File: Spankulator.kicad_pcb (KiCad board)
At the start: 4 copper layers, 50.5 x 110 mm, 97 parts, among them J1 3.5mm Jack, J2 2X8 Header, J3 3.5mm Jack, J4 3.5mm Jack, J5 3.5mm Jack, J6 3.5mm Jack, J7 Expansion Header, J8 FRAM Header, J9 Display Header, Q1 ZVN4206A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

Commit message: v2.2.3
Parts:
- added Q6: TN2106, digikey-footprints:TO-92-3_Formed_Leads, F.Cu at (113.0, 142.1)
- added R21: 10K, Resistor_THT:R_Axial_DIN0207_L6.3mm_D2.5mm_P10.16mm_Horizontal, F.Cu at (113.0, 134.0)
- Q1: value ZVN4206A -> TN2106
- Q2, Q3, Q4, Q5: footprint Package_TO_SOT_THT:TO-92_Inline -> Package_TO_SOT_THT:TO-92_HandSolder
- RV1: value 10K -> 1K
- moved D15 15.4 mm to (58.0, 132.8), turned to 270 degrees
- moved RV1 10.5 mm to (71.1, 144.0), turned to 90 degrees
- moved D3 2.54 mm to (106.2, 48.0), turned to 0 degrees
- moved D4 2.54 mm to (106.2, 78.0), turned to 0 degrees
- moved C13 2.47 mm to (76.6, 132.8)
- moved C3 2.25 mm to (64.0, 51.2)
- moved Q2 0.25 mm to (86.3, 65.5)
- moved Q5 0.20 mm to (86.3, 54.4)
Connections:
- D3 pad 1: GND -> Net-(D3-Pad1)
- D3 pad 2: Net-(D3-Pad2) -> +3V3
- D4 pad 1: GND -> Net-(D4-Pad1)
- D4 pad 2: Net-(D4-Pad2) -> +3V3
- J7 pad 1: Net-(A1-Pad16) -> Net-(J7-Pad1)
- R2 pad 2: Net-(D3-Pad2) -> Net-(D3-Pad1)
- R3 pad 2: Net-(D4-Pad2) -> Net-(D4-Pad1)
- U2 pad 5: +5V -> Net-(Q6-Pad3)
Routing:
- net Net-(A1-Pad16): track 92.9 -> 38.5 mm
- net Net-(D3-Pad2): track 45.4 -> 0.00 mm, vias 2 -> 0
- net Net-(D3-Pad1): track 0.00 -> 45.4 mm, vias 0 -> 2
- net Net-(D4-Pad2): track 44.3 -> 0.00 mm, vias 1 -> 0
- net Net-(D4-Pad1): track 0.00 -> 44.3 mm, vias 0 -> 1
- net Net-(Q6-Pad3): track 0.00 -> 20.2 mm
- net Net-(A1-Pad21): track 80.0 -> 99.6 mm, vias 5 -> 6
- net Net-(A1-Pad20): track 69.5 -> 83.4 mm, vias 1 -> 2
- net +3V3: track 79.7 -> 92.4 mm, vias 10 -> 11
- net /Down: track 103.5 -> 95.5 mm
- net +5V: track 242.3 -> 239.6 mm, vias 7 -> 6
- net /Up: track 116.4 -> 114.1 mm
- net Net-(Q4-Pad2): track 3.39 -> 4.66 mm
- net Net-(Q3-Pad2): track 5.00 -> 6.27 mm
- net Net-(Q2-Pad2): track 9.11 -> 7.84 mm
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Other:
- board size 50.5 x 110 mm -> 60.4 x 110 mm
- board text added: "v2.2"
- board text removed: "v2.1"

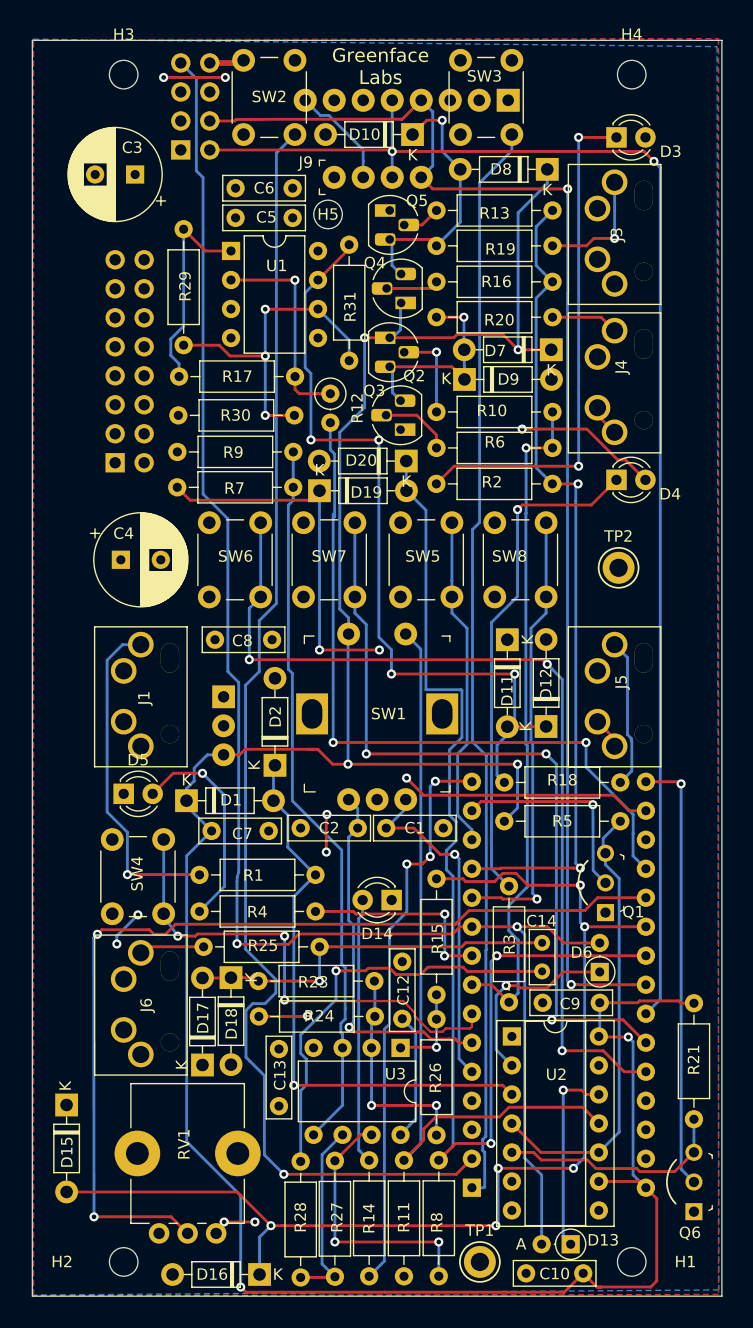
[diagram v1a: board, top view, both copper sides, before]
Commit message: This version adds separate control of external trigger enable. Now uses full-width main board.
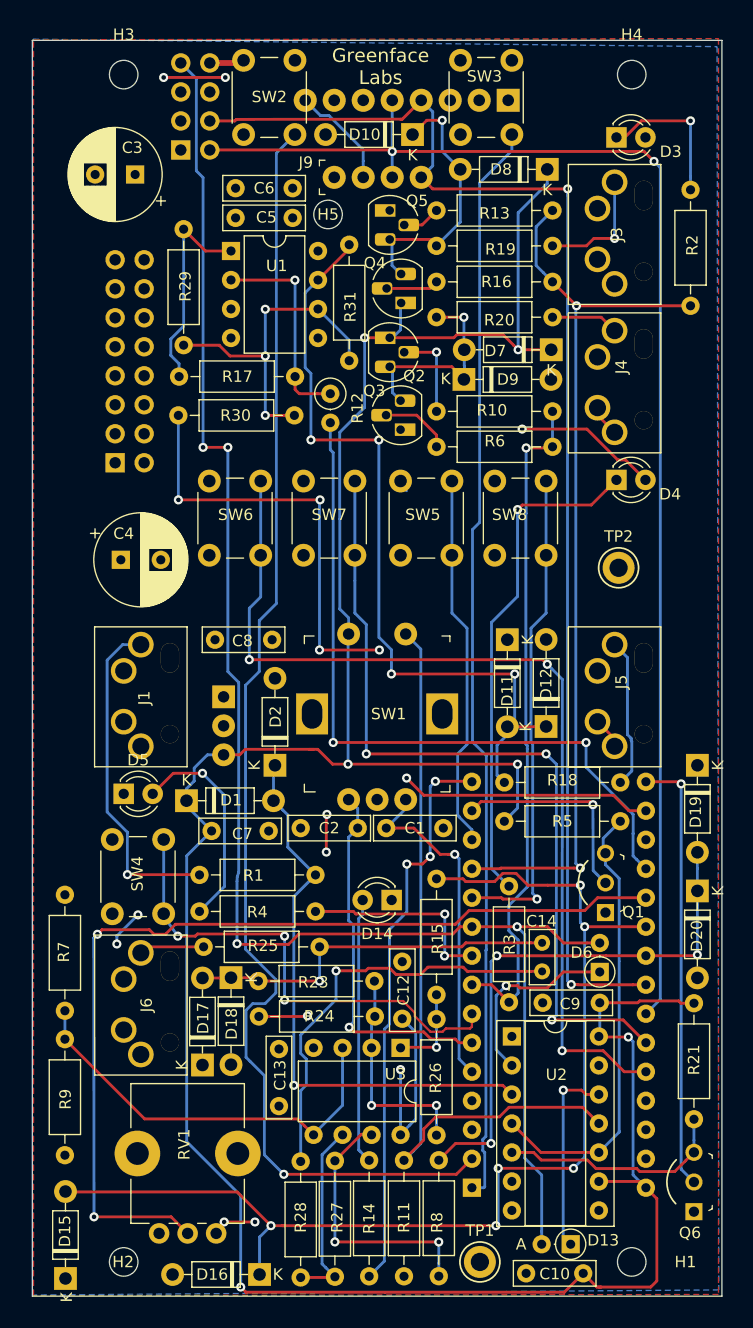
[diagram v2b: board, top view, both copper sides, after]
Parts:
- moved R9 62.4 mm to (57.9, 137.2), turned to 90 degrees
- moved R7 50.0 mm to (57.9, 124.5), turned to 90 degrees
- moved D20 45.5 mm to (113.2, 114.0), turned to 270 degrees
- moved D19 40.9 mm to (113.2, 103.0), turned to 270 degrees
- moved R2 19.7 mm to (112.7, 62.8), turned to 90 degrees
- moved D15 15.2 mm to (57.9, 147.9), turned to 90 degrees
- moved SW5 3.65 mm to (87.2, 84.6)
- moved SW6 3.65 mm to (70.5, 84.6)
- moved SW7 3.65 mm to (78.8, 84.6)
- moved SW8 3.65 mm to (95.5, 84.6)
- moved R6 0.10 mm to (90.4, 75.1)
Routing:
- net Net-(A1-Pad22): track 101.8 -> 48.4 mm, vias 2 -> 3
- net Net-(D3-Pad1): track 45.4 -> 13.4 mm, vias 2 -> 1
- net 1.65V: track 63.3 -> 36.4 mm
- net Net-(A1-Pad12): track 72.1 -> 79.4 mm
- net +3V3: track 92.4 -> 98.1 mm, vias 11 -> 13
- net +12V: track 14.5 -> 20.2 mm, vias 2 -> 3
- net /Param+: track 39.5 -> 44.3 mm
- net /Param-: track 29.2 -> 32.8 mm
- net /Right: track 81.2 -> 84.8 mm
- net /Left: track 69.3 -> 73.0 mm
- net /Trigger: track 141.0 -> 142.3 mm, vias 2 -> 4

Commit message: Ver 2.3
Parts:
- added H6: MountingHole, sputterizer:MountingHole_2.5mm-No-Margin, F.Cu at (73.5, 76.0)
- added H7: MountingHole, sputterizer:MountingHole_2.5mm-No-Margin, F.Cu at (96.8, 76.0)
- D13, D6: footprint Diode_THT:D_DO-35_SOD27_P2.54mm_Vertical_AnodeUp -> Diode_THT:D_DO-35_SOD27_P7.62mm_Horizontal
- R12: footprint Resistor_THT:R_Axial_DIN0207_L6.3mm_D2.5mm_P2.54mm_Vertical -> Resistor_THT:R_Axial_DIN0207_L6.3mm_D2.5mm_P10.16mm_Horizontal
- moved R6 23.3 mm to (112.7, 82.1), turned to 90 degrees
- moved D6 22.9 mm to (113.1, 99.8)
- moved TP1 18.4 mm to (112.6, 146.6)
- moved R12 17.8 mm to (66.5, 60.2)
- moved R17 13.5 mm to (69.6, 55.6), turned to 270 degrees
- moved R29 11.7 mm to (79.7, 68.8), turned to 180 degrees
- moved J2 4.14 mm to (58.1, 76.1)
- moved R30 1.84 mm to (79.7, 71.8)
- moved SW5 1.00 mm to (87.2, 85.6)
- moved SW6 1.00 mm to (70.5, 85.6)
- moved SW7 1.00 mm to (78.8, 85.6)
- moved SW8 1.00 mm to (95.5, 85.6)
- moved D13 0.65 mm to (101.5, 145.0)
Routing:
- net /Trigger: track 142.3 -> 189.6 mm, vias 4 -> 6
- net Net-(D6-Pad1): track 16.8 -> 45.6 mm, vias 1 -> 2
- net +3V3: track 98.1 -> 69.7 mm, vias 13 -> 8
- net Net-(Q3-Pad2): track 6.27 -> 34.4 mm, vias 0 -> 1
- net Net-(R29-Pad1): track 29.7 -> 12.3 mm, vias 3 -> 0
- net Net-(A1-Pad19): track 64.2 -> 81.5 mm, vias 2 -> 3
- net Net-(A1-Pad8): track 59.3 -> 71.5 mm, vias 1 -> 0
- net +5V: track 239.6 -> 232.3 mm
- net Net-(R12-Pad1): track 18.4 -> 12.4 mm, vias 1 -> 0
- net /Param+: track 44.3 -> 43.1 mm
- net Net-(D11-Pad2): track 70.1 -> 70.8 mm
- net Net-(D4-Pad1): track 44.3 -> 45.0 mm
- net Net-(R17-Pad1): track 18.6 -> 18.1 mm
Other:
- board text added: "v2.3"
- board text removed: "v2.2"

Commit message: ver 3.0
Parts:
- removed D10, D17, D18, D2, D9: SB120, sputterizer:D_DO-41_SOD27_P7.62mm_Horizontal
- removed Q2, Q4: 2N3906, Package_TO_SOT_THT:TO-92_HandSolder
- removed R13: 100K, Resistor_THT:R_Axial_DIN0207_L6.3mm_D2.5mm_P10.16mm_Horizontal
- removed R25: 470, Resistor_THT:R_Axial_DIN0207_L6.3mm_D2.5mm_P10.16mm_Horizontal
- added C11: 2.2uF, Capacitor_THT:C_Rect_L7.0mm_W2.0mm_P5.00mm, F.Cu at (56.9, 109.6)
- added C15: 2.2uF, Capacitor_THT:C_Rect_L7.0mm_W2.0mm_P5.00mm, F.Cu at (57.3, 101.5)
- added C16: 270p, Capacitor_THT:C_Rect_L4.0mm_W2.5mm_P2.50mm, F.Cu at (65.5, 78.6)
- added C17: 100nF, Capacitor_THT:C_Rect_L7.0mm_W2.0mm_P5.00mm, F.Cu at (57.5, 78.4)
- added U5: LP2950-3.3_TO92, Package_TO_SOT_THT:TO-92_Inline, F.Cu at (58.4, 106.8)
- added U6: MAX7480, Package_DIP:DIP-8_W7.62mm_Socket_LongPads, F.Cu at (57.5, 81.5)
- A1: value Arduino_Nano_33IoT -> Nano_33IoT
- D1, D15, D16, D19, D20: value SB120 -> BAT46; footprint sputterizer:D_DO-41_SOD27_P7.62mm_Horizontal -> Diode_THT:D_DO-35_SOD27_P7.62mm_Horizontal
- J2: value 2X8 Header -> 2x5 Header; footprint Connector_PinHeader_2.54mm:PinHeader_2x08_P2.54mm_Vertical -> Connector_PinHeader_2.54mm:PinHeader_2x05_P2.54mm_Vertical
- Q3, Q5: value 2N3904 -> TN2106; footprint Package_TO_SOT_THT:TO-92_HandSolder -> digikey-footprints:TO-92-3_Formed_Leads
- R10, R16: value 47K -> 470
- R12, R26, R27: value 100K -> 100K .1%
- R29, R31: value 200K -> 100K .1%
- R30: value 133K -> 100K .1%
- R6: value 100K -> 10K
- R7, R9: value 470 -> 510 .1%
- SW2, SW3, SW4, SW5, SW6, SW7, SW8: value ~ -> Push Button
- TP2: moved to B.Cu
- moved R8 60.0 mm to (80.2, 88.7), turned to 180 degrees
- moved J8 55.8 mm to (113.5, 98.0), turned to 90 degrees
- moved D1 44.8 mm to (113.2, 104.0), turned to 270 degrees
- moved TP2 41.0 mm to (101.6, 44.9)
- moved D20 38.1 mm to (76.0, 106.0), turned to 180 degrees
- moved D19 38.0 mm to (75.9, 96.0)
- moved H5 35.6 mm to (103.5, 82.2), turned to 270 degrees
- moved C14 28.4 mm to (72.2, 126.0)
- moved C4 26.9 mm to (58.0, 58.5)
- moved D6 21.7 mm to (113.2, 121.5)
- moved R6 19.0 mm to (94.9, 88.8), turned to 0 degrees
- moved R10 15.2 mm to (100.6, 60.7), turned to 180 degrees
- moved R31 11.3 mm to (82.8, 68.7), turned to 90 degrees
- moved R7 11.0 mm to (57.0, 135.5)
- moved R9 10.9 mm to (57.0, 148.0)
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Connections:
- A1 pad 18: Net-(A1-Pad18) -> 3.3VRef
- A1 pad 21: Net-(A1-Pad21) -> SigIn
- A1 pad 3: Net-(A1-Pad3) -> Reset
- D1 pad 1: +5V -> +3V3
- D1 pad 2: Net-(D1-Pad2) -> Net-(A1-Pad22)
- D15 pad 2: Net-(A1-Pad21) -> SigIn
- D16 pad 1: Net-(A1-Pad21) -> SigIn
- D19 pad 1: +3V3 -> +5V
- D19 pad 2: Net-(A1-Pad22) -> Net-(D19-Pad2)
- D20 pad 1: Net-(A1-Pad22) -> Net-(D19-Pad2)
- D8 pad 2: Net-(D10-Pad1) -> Net-(D8-Pad2)
- J6 pad 2: Net-(J6-Pad2) -> Net-(C14-Pad1)
- J7 pad 1: Net-(J7-Pad1) -> Reset
- J7 pad 3: +3V3 -> SigIn
- Q3 pad 2: Net-(Q3-Pad2) -> Net-(A1-Pad8)
- Q5 pad 2: Net-(Q5-Pad2) -> Net-(A1-Pad12)
- Q5 pad 3: Net-(D10-Pad1) -> Net-(D8-Pad2)
- R1 pad 1: Net-(D1-Pad2) -> Net-(R1-Pad1)
- R10 pad 1: Net-(Q2-Pad2) -> +5V
- R10 pad 2: Net-(A1-Pad8) -> Net-(D7-Pad2)
- R15 pad 2: Net-(A1-Pad21) -> SigIn
- R16 pad 1: Net-(Q4-Pad2) -> +5V
- R16 pad 2: Net-(A1-Pad12) -> Net-(D8-Pad2)
- R17 pad 1: Net-(R17-Pad1) -> Net-(D11-Pad2)
- R19 pad 1: Net-(D10-Pad1) -> Net-(D8-Pad2)
- R24 pad 2: +3V3 -> 3.3VRef
- R29 pad 2: Net-(R17-Pad1) -> 1.65V
- R30 pad 1: Net-(R29-Pad1) -> Net-(R12-Pad1)
- R30 pad 2: +3V3 -> Net-(R30-Pad2)
- R31 pad 1: Net-(D11-Pad2) -> Net-(R30-Pad2)
- R6 pad 1: Net-(Q3-Pad2) -> Net-(R6-Pad1)
- R6 pad 2: Net-(A1-Pad8) -> Net-(A1-Pad22)
- R7 pad 2: +3V3 -> 3.3VRef
- R8 pad 2: Net-(A1-Pad22) -> Net-(D19-Pad2)
- RV1 pad 1: +3V3 -> 3.3VRef
- U1 pad 1: Net-(R17-Pad1) -> Net-(D11-Pad2)
- U1 pad 7: Net-(D11-Pad2) -> Net-(R30-Pad2)
- U2 pad 3: Net-(D1-Pad2) -> Net-(R1-Pad1)
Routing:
- net SigIn: track 0.00 -> 170.0 mm, vias 0 -> 7
- net Reset: track 0.00 -> 109.7 mm, vias 0 -> 2
- net 3.3VRef: track 0.00 -> 103.5 mm, vias 0 -> 1
- net Net-(A1-Pad21): track 99.6 -> 0.00 mm, vias 6 -> 0
- net 1.65V: track 36.4 -> 122.9 mm, vias 0 -> 3
- net +3V3: track 69.7 -> 13.7 mm, vias 8 -> 5
- net Net-(D1-Pad2): track 49.8 -> 0.00 mm, vias 1 -> 0
- net Net-(R1-Pad1): track 0.00 -> 38.6 mm, vias 0 -> 1
- net Net-(D19-Pad2): track 0.00 -> 38.0 mm, vias 0 -> 1
- net Net-(Q3-Pad2): track 34.4 -> 0.00 mm, vias 1 -> 0
- net Net-(R27-Pad2): track 23.5 -> 55.8 mm, vias 2 -> 0
- net Net-(R6-Pad1): track 0.00 -> 30.4 mm
- net /Trigger: track 189.6 -> 165.5 mm
- net Net-(D10-Pad1): track 23.1 -> 0.00 mm, vias 1 -> 0
- net Net-(C14-Pad2): track 37.2 -> 14.4 mm
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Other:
- board text added: "v3.0"
- board text removed: "Pin 1 -12V"
- board text removed: "v2.3"

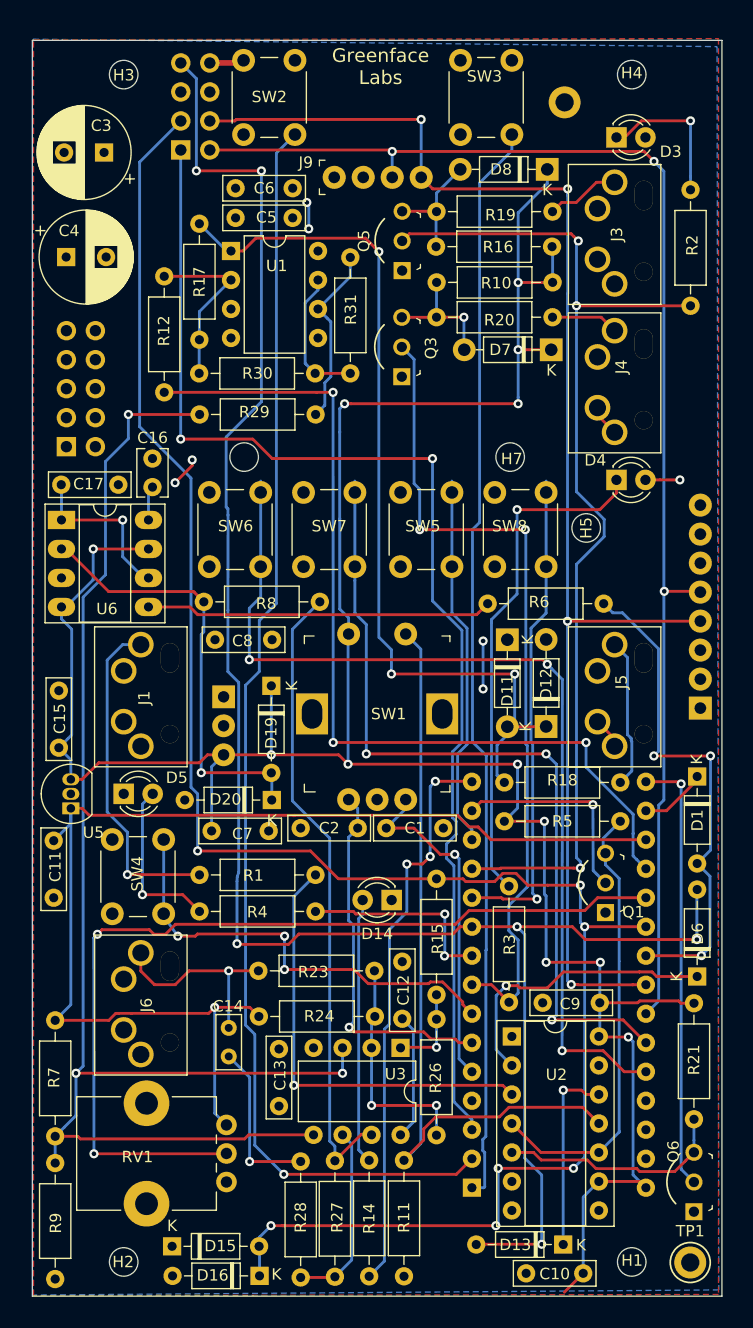
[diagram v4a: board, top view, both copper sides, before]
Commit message: Version 3.1
Adds adjustment pots.
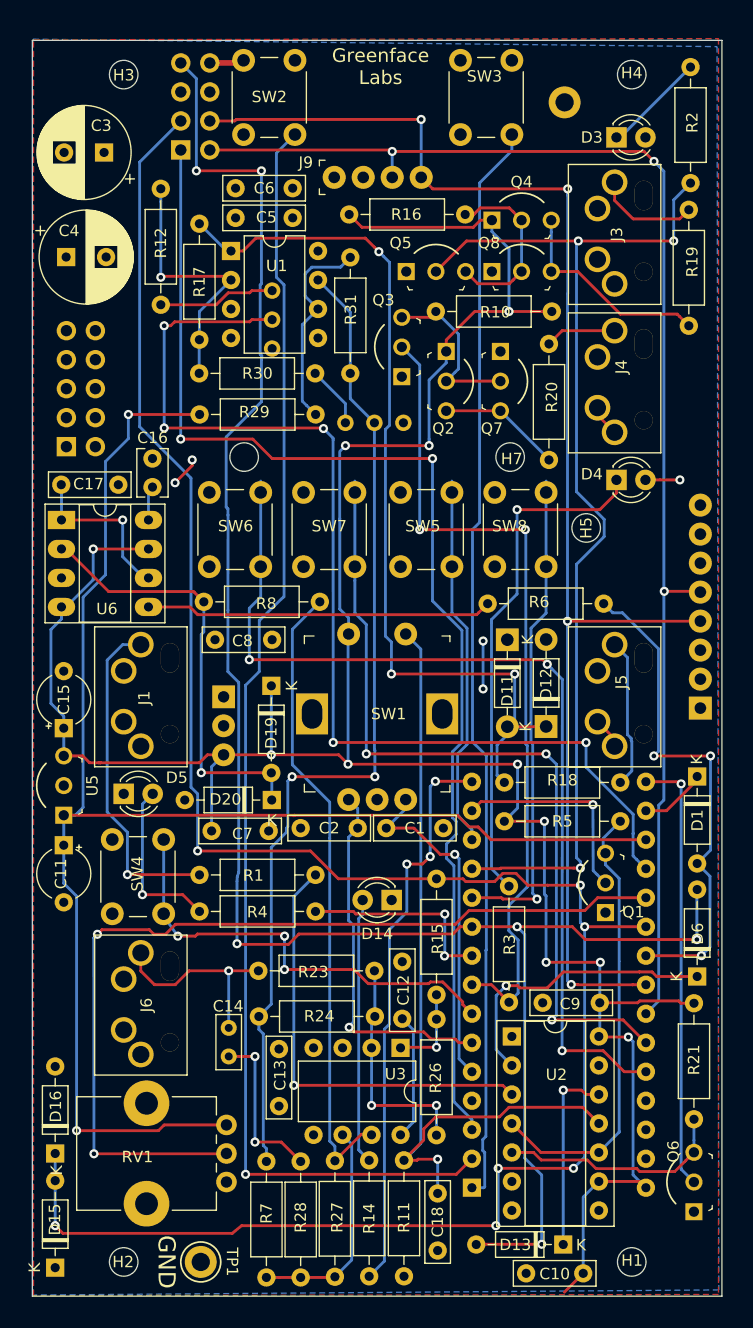
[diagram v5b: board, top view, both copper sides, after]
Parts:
- removed D7, D8: SB120, sputterizer:D_DO-41_SOD27_P7.62mm_Horizontal
- removed R9: 510 .1%, Resistor_THT:R_Axial_DIN0207_L6.3mm_D2.5mm_P10.16mm_Horizontal
- added C18: 10nF, Capacitor_THT:C_Rect_L7.0mm_W2.0mm_P5.00mm, F.Cu at (90.5, 140.5)
- added Q2: VP2106, digikey-footprints:TO-92-3_Formed_Leads, F.Cu at (91.2, 66.8)
- added Q4: VP2106, digikey-footprints:TO-92-3_Formed_Leads, F.Cu at (95.2, 55.2)
- added Q7: TN2106, digikey-footprints:TO-92-3_Formed_Leads, F.Cu at (96.0, 66.8)
- added Q8: TN2106, digikey-footprints:TO-92-3_Formed_Leads, F.Cu at (95.2, 59.8)
- added RV2: 10K, Potentiometer_THT:Potentiometer_Bourns_3266Y_Vertical, B.Cu at (76.0, 66.5)
- added RV3: 10K, Potentiometer_THT:Potentiometer_Bourns_3266Y_Vertical, B.Cu at (87.5, 73.0)
- C11, C15: footprint Capacitor_THT:C_Rect_L7.0mm_W2.0mm_P5.00mm -> sputterizer:CP_Radial_Tantal_D4.5mm_P5.00mm_Min
- R10, R16: value 470 -> 100K
- R12, R30: value 100K .1% -> 95.3K 1%
- R17, R23, R28: value 301K -> 300K .1%
- R24: value 301K -> 100K .1%
- R29: value 100K .1% -> 200K .1%
- R7: value 510 .1% -> 100K .1%
- U5: footprint Package_TO_SOT_THT:TO-92_Inline -> digikey-footprints:TO-92-3_Formed_Leads
- moved TP1 42.9 mm to (69.8, 146.5)
- moved R19 24.3 mm to (112.5, 64.5), turned to 90 degrees
- moved R7 22.2 mm to (75.5, 147.9)
- moved D16 20.9 mm to (57.0, 137.0), turned to 90 degrees
- moved R16 18.0 mm to (82.8, 54.8), turned to 0 degrees
- moved R20 15.9 mm to (100.2, 76.2), turned to 90 degrees
- moved R2 10.8 mm to (112.7, 52.0)
- moved D15 10.4 mm to (57.0, 147.0), turned to 90 degrees
- moved R12 7.68 mm to (66.2, 52.5)
- moved R10 2.55 mm to (100.5, 63.2)
- moved C15 1.76 mm to (57.8, 99.8)
- moved C11 0.97 mm to (57.8, 110.0)
- moved U5 0.87 mm to (57.8, 107.4)
- moved Q5 0.37 mm to (87.8, 59.8), turned to 0 degrees
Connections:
- net /Down renamed /FXN-
- net /Left renamed /Down(v)
- net /Param+ renamed /Right(>)
- net /Param- renamed /Left(<)
- net /Right renamed /Up(^)
- net /Up renamed /FXN+
- Q3 pad 3: Net-(D7-Pad2) -> Net-(Q2-Pad2)
- Q5 pad 3: Net-(D8-Pad2) -> Net-(Q4-Pad2)
- R10 pad 2: Net-(D7-Pad2) -> Net-(Q2-Pad2)
- R12 pad 2: Net-(A1-Pad19) -> Net-(R12-Pad2)
- R16 pad 2: Net-(D8-Pad2) -> Net-(Q4-Pad2)
- R19 pad 1: Net-(D8-Pad2) -> Net-(Q4-Pad3)
- R20 pad 1: Net-(D7-Pad2) -> Net-(Q2-Pad3)
- R24 pad 2: 3.3VRef -> -1.65V
- R29 pad 2: 1.65V -> 3.3VRef
- R31 pad 1: Net-(R30-Pad2) -> -1.65V
- R7 pad 1: 1.65V -> Net-(R27-Pad1)
- R7 pad 2: 3.3VRef -> -1.65V
- U1 pad 7: Net-(R30-Pad2) -> -1.65V
- U3 pad 3: 1.65V -> GND
- U3 pad 5: 1.65V -> GND
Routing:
- net 1.65V: track 122.9 -> 0.00 mm, vias 3 -> 0
- net -1.65V: track 0.00 -> 88.0 mm, vias 0 -> 2
- net 3.3VRef: track 103.5 -> 137.0 mm, vias 1 -> 2
- net SigIn: track 170.0 -> 190.8 mm
- net Net-(Q4-Pad3): track 0.00 -> 18.5 mm
- net Net-(Q4-Pad2): track 0.00 -> 15.9 mm
- net Net-(Q2-Pad2): track 0.00 -> 15.3 mm
- net Net-(A1-Pad19): track 81.5 -> 96.4 mm, vias 3 -> 5
- net Net-(D7-Pad2): track 11.4 -> 0.00 mm, vias 1 -> 0
- net Net-(Q2-Pad3): track 0.00 -> 10.8 mm
- net Net-(D8-Pad2): track 10.7 -> 0.00 mm
- net Net-(R12-Pad2): track 0.00 -> 10.3 mm
- net Net-(R12-Pad1): track 15.3 -> 23.1 mm, vias 0 -> 1
- net Net-(R30-Pad2): track 12.1 -> 5.43 mm
- net Net-(C18-Pad1): track 67.6 -> 73.5 mm, vias 0 -> 1
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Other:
- board text added: "Exp"
- board text added: "GAIN"
- board text added: "GND"
- board text added: "OFFSET"
- board text added: "POWER"
- board text added: "v3.1"
- board text removed: "v3.0"
